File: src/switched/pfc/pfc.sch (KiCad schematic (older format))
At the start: 67 parts, among them J1 AC-input, J2 Conn_01x02, J3 Conn_01x02, Q1 AOT190A60CL‎, U1 AP3917B, U2 bd7692fj

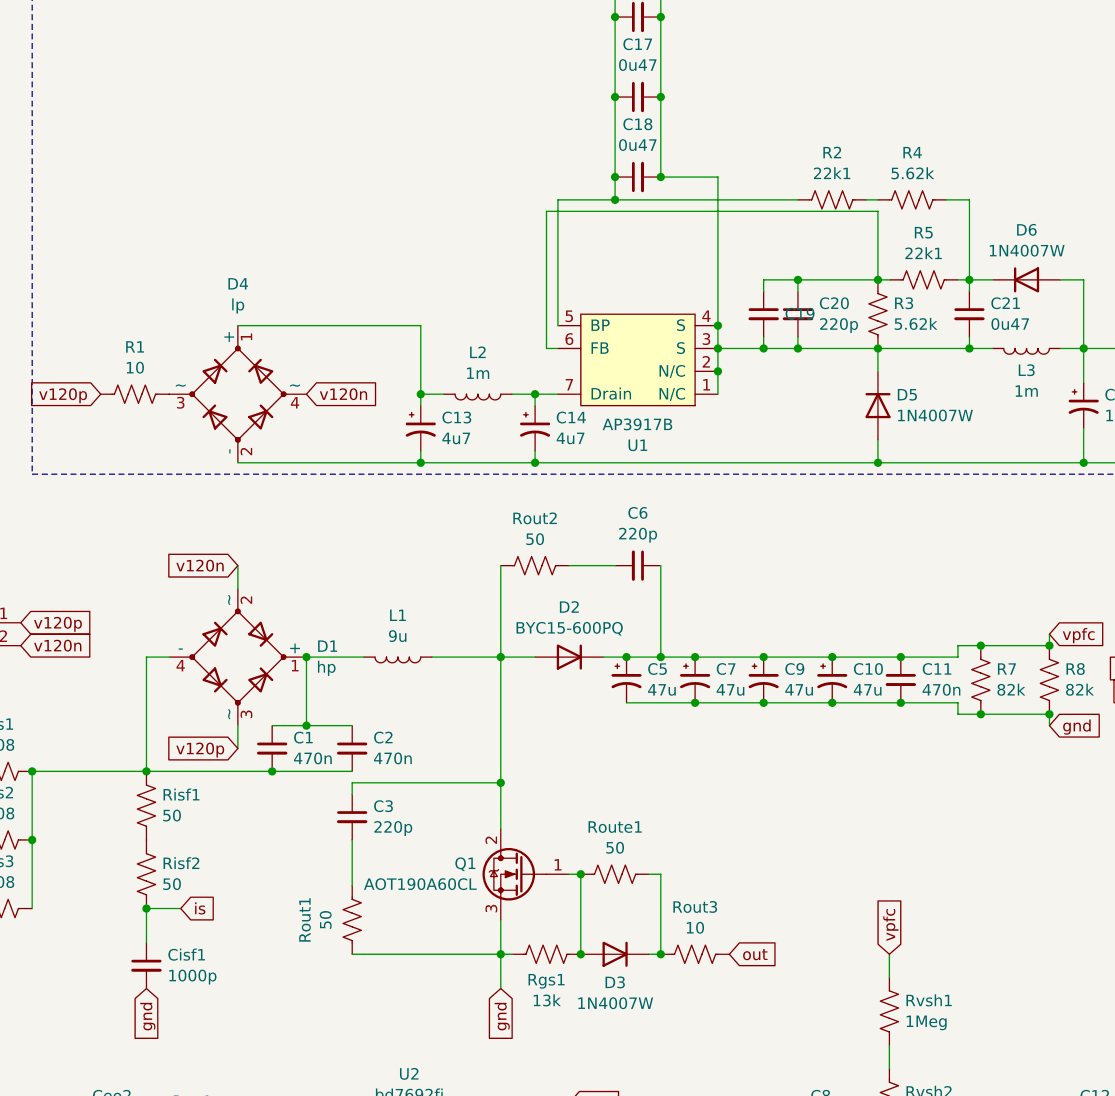
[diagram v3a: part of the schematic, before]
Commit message: fixing the pfc footprints and relating them to their lcsc counterparts
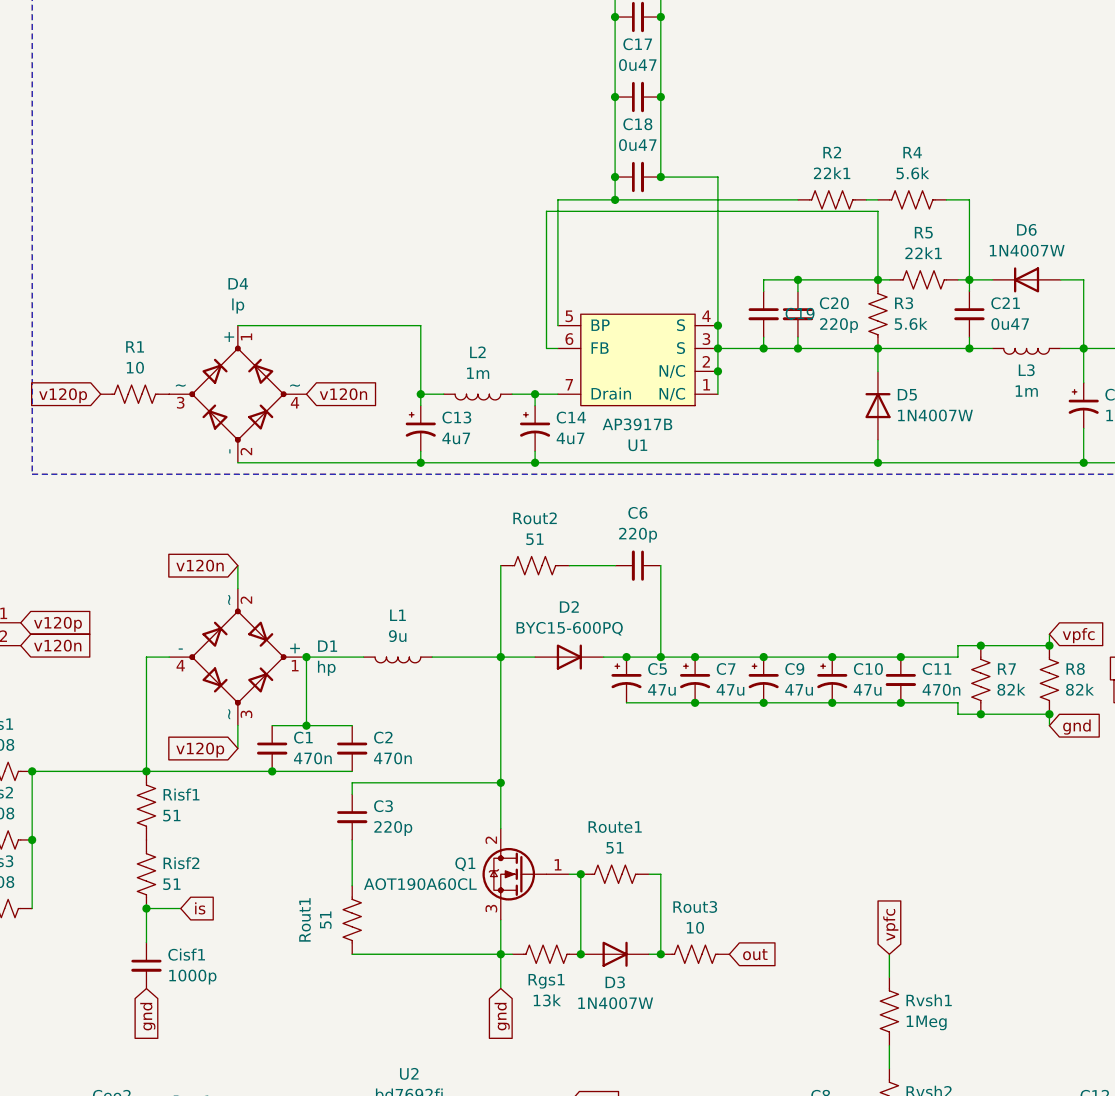
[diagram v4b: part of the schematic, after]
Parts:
- C1, C11, C2: footprint Capacitor_SMD:C_1812_4532Metric_Pad1.57x3.40mm_HandSolder -> Capacitor_SMD:C_1812_4532Metric; Checked yes -> (none); Link (none) -> https://lcsc.com/product-detail/Multilayer-Ceramic-Capacito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; link https://lcsc.com/product-detail/Multilayer-Ceramic-Capacito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 -> (none)
- C10, C5, C7, C9: Link (none) -> https://lcsc.com/product-detail/Aluminum-Electrolytic-Capac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; Working voltage (none) -> 450; link https://lcsc.com/product-detail/Aluminum-Electrolytic-Capac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 -> (none)
- C12, C8, Ceo2, Cisf1: Link (none) -> https://lcsc.com/product-detail/Multilayer-Ceramic-Capacito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; Working voltage (none) -> 50
- C13, C14: Link (none) -> https://lcsc.com/product-detail/Aluminum-Electrolytic-Capac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; Working voltage (none) -> 400; price (none) -> 0.039
- C15, C16, C17, C18, C21, Ceo1: Link (none) -> https://lcsc.com/search?q=CL10B474KA8NNNC; Working voltage (none) -> 25
- C19, C20, C3, C6: Checked yes -> (none); Link (none) -> https://lcsc.com/product-detail/Multilayer-Ceramic-Capacito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; link https://lcsc.com/product-detail/Multilayer-Ceramic-Capacito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 -> (none)
- C22: Link (none) -> https://lcsc.com/product-detail/Aluminum-Electrolytic-Capac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; Working voltage (none) -> 25; price (none) -> 0.0308
- C4: Link (none) -> https://lcsc.com/product-detail/Aluminum-Electrolytic-Capac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; link https://lcsc.com/product-detail/Aluminum-Electrolytic-Capac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 -> (none)
- D1: Link (none) -> https://lcsc.com/product-detail/Bridge-Rectifiers_Yangzhou-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
- D2: Link (none) -> https://lcsc.com/product-detail/Diodes-General-Purpose_WeEn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
- D3, D5, D6: Link (none) -> https://lcsc.com/product-detail/Diodes-General-Purpose_Shan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
- D4: Link (none) -> https://lcsc.com/product-detail/Bridge-Rectifiers_DIYI-Elec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; price 0.6459 -> 0.0342
- J1, J3: Checked (none) -> NA; Link (none) -> NA
- J2: footprint Connector_Wire:SolderWire-2sqmm_1x02_P7.8mm_D2mm_OD3.9mm -> custom:spacedConnector; Checked (none) -> NA; Link (none) -> NA
- L1: Link (none) -> https://www.digikey.com/en/products/detail/ferroxcube/CPV-P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
- L2, L3: Link (none) -> https://lcsc.com/product-detail/Power-Inductors_YJYCOIN-YNR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; price (none) -> 0.0974
- Q1: footprint Package_TO_SOT_THT:TO-220-2_Horizontal_TabDown -> Package_TO_SOT_THT:TO-220-3_Horizontal_TabDown; Link (none) -> https://www.digikey.com/en/products/detail/alpha-omega-semi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; price 2.5648 -> 2.17
- R1: Link (none) -> https://lcsc.com/product-detail/Wirewound-Resistors_CCO-Chi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; Working voltage (none) -> 300; price (none) -> 0.0443
- R2, R5, R6: Link (none) -> https://lcsc.com/product-detail/Metal-Oxide-Resistors_FlyWi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; Working voltage (none) -> 250; price (none) -> 0.0041
- R3, R4: value 5.62k -> 5.6k; footprint Resistor_THT:R_Axial_DIN0309_L9.0mm_D3.2mm_P2.54mm_Vertical -> Resistor_THT:R_Axial_DIN0204_L3.6mm_D1.6mm_P2.54mm_Vertical; Link (none) -> https://lcsc.com/product-detail/Metal-Film-Resistor-TH_5-6K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; Working voltage (none) -> 150; price (none) -> 0.0087
- R7, R8: Link (none) -> https://lcsc.com/product-detail/Metal-Oxide-Resistors_FlyWi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; Working voltage (none) -> 500; price (none) -> 0.0487
- Reo1, Rt1: Link (none) -> https://lcsc.com/product-detail/High-Precision-Low-TCR-SMD-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; Working voltage (none) -> 75
- Rgs1, Rovpl1, Rvsl1, Rvsl2: Link (none) -> https://lcsc.com/product-detail/Chip-Resistor-Surface-Mount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; Working voltage (none) -> 50
- Ris1, Ris2, Ris3: Link (none) -> https://lcsc.com/product-detail/Low-Resistors-Current-Sense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
- Risf1, Risf2, Route1: value 50 -> 51; Link (none) -> https://lcsc.com/product-detail/Carbon-Film-Resistors_Huaxi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; Working voltage (none) -> 250
- Rout1, Rout2: value 50 -> 51; footprint Resistor_SMD:R_1206_3216Metric_Pad1.30x1.75mm_HandSolder -> Resistor_THT:R_Axial_DIN0207_L6.3mm_D2.5mm_P10.16mm_Horizontal; Link (none) -> https://lcsc.com/product-detail/Carbon-Film-Resistors_Huaxi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; Working voltage (none) -> 250
- Rout3: Link (none) -> https://lcsc.com/product-detail/Chip-Resistor-Surface-Mount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; Working voltage (none) -> 75
- Rovph1, Rovph2, Rvsh1, Rvsh2: Link (none) -> https://lcsc.com/product-detail/High-Voltage-Resistor_Ever-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; Working voltage (none) -> 500
- U1: footprint custom:SO-7_5.3x6.2mm_P1.27mm -> custom:SO-7_3.9x4.9mm_P1.27mm; Link (none) -> https://www.digikey.com/en/products/detail/AP3917BS7-13/AP3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; price (none) -> 0.58000
- U2: footprint Package_SO:SOP-8_6.62x9.15mm_P2.54mm -> Package_SO:SOIC-8_3.9x4.9mm_P1.27mm; Link (none) -> https://www.digikey.com/en/products/detail/BD7692FJ-E2/846-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

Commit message: Midterm report
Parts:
- C1, C11, C2: price 0.0143 -> 0.2238
- C10, C5, C7, C9: price 0.6115 -> 0.4815
- C12, C8, Cisf1: price 0.004 -> 0.0031
- C13, C14: price 0.039 -> 0.039
- C15, C16, C17, C18, C21, Ceo1: price 0.0143 -> 0.0112
- C19, C20, C3, C6: price 0.016 -> 0.0126
- C4: price 0.0125 -> 0.0098
- Ceo2: price 0.0041 -> 0.0032
- D1: price 0.6459 -> 0.5086
- D2: price 0.9091 -> 0.7159
- D3, D5, D6: price 0.0086 -> 0.0067
- D4: price 0.0342 -> 0.0271
- L2, L3: price 0.0974 -> 0.0772
- R1: price 0.0443 -> 0.0351
- R2, R5, R6: price 0.0041 -> 0.0041
- R3, R4: price 0.0087 -> 0.0052
- Reo1, Rt1: price 0.0091 -> 0.0071
- Rgs1, Rovpl1, Rvsl1, Rvsl2: price 0.0014 -> 0.0011
- Ris1, Ris2, Ris3: price 0.093 -> 0.0732
- Risf1, Risf2, Rout1, Rout2, Route1: price 0.0064 -> 0.005
- Rout3: price 0.0016 -> 0.0012
- Rovph1, Rovph2, Rvsh1, Rvsh2: price 0.0298 -> 0.0234
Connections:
- net v12 renamed vcc
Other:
- moved on the sheet: C1, C10, C11, C12, C13, C14, C15, C16, C17, C18, C19, C2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

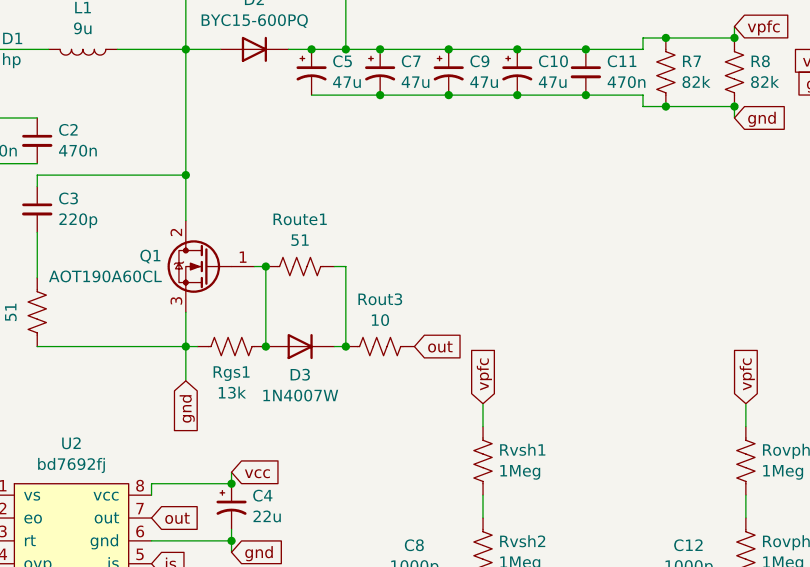
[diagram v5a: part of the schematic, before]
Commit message: Faster gate drive on pfc
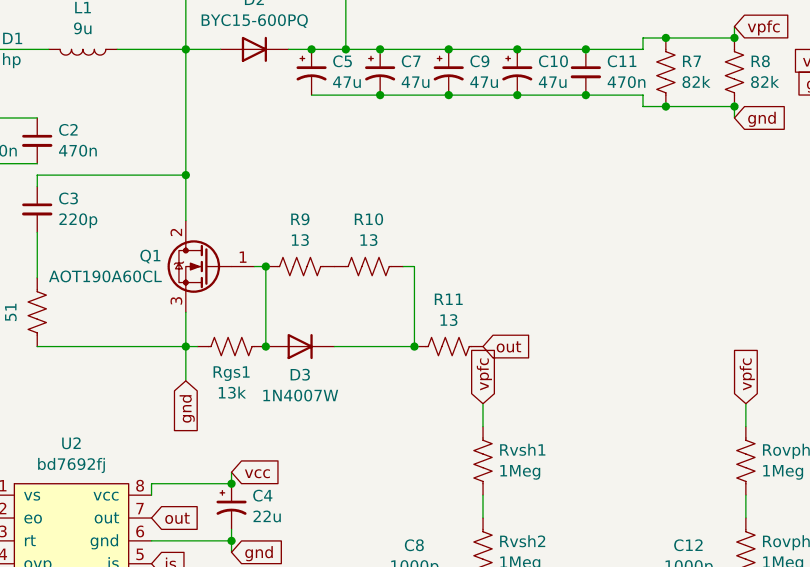
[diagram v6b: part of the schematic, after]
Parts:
- removed Route1: 51, Resistor_THT:R_Axial_DIN0207_L6.3mm_D2.5mm_P2.54mm_Vertical, symbol Device:R_US
- added R10, R9: 13, Resistor_SMD:R_0603_1608Metric_Pad0.98x0.95mm_HandSolder, symbol Device:R_US
- R11: renamed from Rout3; value 10 -> 13; Link https://lcsc.com/product-detail/Chip-Resistor-Surface-Mount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 -> https://lcsc.com/product-detail/High-Precision-Low-TCR-SMD-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; price 0.0012 -> 0.0119
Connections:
- net at D3.2 (A), Q1.1 (G), Rgs1.2: now also R9.1
- net at D3.1 (K), R11.1: now also R10.2
- new net: R10.1, R9.2
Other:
- moved on the sheet: R11
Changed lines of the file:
@@
 	3700 5350 3700 5700
-$Comp
-L Device:R_US Route1
-U 1 1 6037526C
-P 3850 5350
-F 0 "Route1" V 4055 5350 50  0000 C CNN
-F 1 "51" V 3964 5350 50  0000 C CNN
-F 2 "Resistor_THT:R_Axial_DIN0207_L6.3mm_D2.5mm_P2.54mm_Vertical" V 3890 5340 50  0001 C CNN
-F 3 "CF1/4W-51Ω±5%T52" H 3850 5350 50  0001 C CNN
-F 4 "0.005" H 3850 5350 50  0001 C CNN "price"
-F 5 "" H 3850 5350 50  0001 C CNN "Checked"
-F 6 "https://lcsc.com/product-detail/Carbon-Film-Resistors_Huaxing-Mechanical-Elec-CF1-4W-51%CE%A9-5-T52_C714278.html" H 3850 5350 50  0001 C CNN "Link"
-F 7 "250" H 3850 5350 50  0001 C CNN "Working voltage"
-	1    3850 5350
-	0    -1   -1   0
-$EndComp
 $Comp
 L Device:D D3
@@
 $EndComp
 $Comp
-L Device:R_US Rout3
+L Device:R_US R11
 U 1 1 60379771
-P 4200 5700
-F 0 "Rout3" V 4405 5700 50  0000 C CNN
-F 1 "10" V 4314 5700 50  0000 C CNN
-F 2 "Resistor_SMD:R_0603_1608Metric_Pad0.98x0.95mm_HandSolder" V 4240 5690 50  0001 C CNN
-F 3 "WR06X100JTL" H 4200 5700 50  0001 C CNN
-F 4 "0.0012" H 4200 5700 50  0001 C CNN "price"
-F 5 "" H 4200 5700 50  0001 C CNN "Checked"
-F 6 "https://lcsc.com/product-detail/Chip-Resistor-Surface-Mount_Walsin-Tech-Corp-WR06X100JTL_C384297.html" H 4200 5700 50  0001 C CNN "Link"
-F 7 "75" H 4200 5700 50  0001 C CNN "Working voltage"
-	1    4200 5700
+P 4500 5700
+F 0 "R11" V 4705 5700 50  0000 C CNN
+F 1 "13" V 4614 5700 50  0000 C CNN
+F 2 "Resistor_SMD:R_0603_1608Metric_Pad0.98x0.95mm_HandSolder" V 4540 5690 50  0001 C CNN
+F 3 "ARG03FTC0130" H 4500 5700 50  0001 C CNN
+F 4 "0.0119" H 4500 5700 50  0001 C CNN "price"
+F 5 "" H 4500 5700 50  0001 C CNN "Checked"
+F 6 "https://lcsc.com/product-detail/High-Precision-Low-TCR-SMD-Resistors_Viking-Tech-ARG03FTC0130_C217732.html" H 4500 5700 50  0001 C CNN "Link"
+F 7 "75" H 4500 5700 50  0001 C CNN "Working voltage"
+	1    4500 5700
 	0    -1   -1   0
 $EndComp
-Text GLabel 4350 5700 2    50   Input ~ 0
+Text GLabel 4650 5700 2    50   Input ~ 0
 out
 Wire Wire Line
@@
 	1300 5200 1300 5500
 Wire Wire Line
-	4000 5350 4050 5350
-Wire Wire Line
-	4050 5700 4000 5700
-Wire Wire Line
-	4050 5700 4050 5350
-Connection ~ 4050 5700
+	4300 5350 4350 5350
+Wire Wire Line
+	4350 5700 4350 5350
+Connection ~ 4350 5700
 $Comp
 L Device:R_US Rout1
@@
 Wire Wire Line
 	3350 4950 3350 5150
-Connection ~ 3700 5350
 Connection ~ 3700 5700
 Wire Wire Line
@@
 	1    0    0    -1
 $EndComp
+$Comp
+L Device:R_US R9
+U 1 1 604B894B
+P 3850 5350
+F 0 "R9" V 4055 5350 50  0000 C CNN
+F 1 "13" V 3964 5350 50  0000 C CNN
+F 2 "Resistor_SMD:R_0603_1608Metric_Pad0.98x0.95mm_HandSolder" V 3890 5340 50  0001 C CNN
+F 3 "ARG03FTC0130" H 3850 5350 50  0001 C CNN
+F 4 "0.0119" H 3850 5350 50  0001 C CNN "price"
+F 5 "" H 3850 5350 50  0001 C CNN "Checked"
+F 6 "https://lcsc.com/product-detail/High-Precision-Low-TCR-SMD-Resistors_Viking-Tech-ARG03FTC0130_C217732.html" H 3850 5350 50  0001 C CNN "Link"
+F 7 "75" H 3850 5350 50  0001 C CNN "Working voltage"
+	1    3850 5350
+	0    -1   -1   0
+$EndComp
+Connection ~ 3700 5350
+$Comp
+L Device:R_US R10
+U 1 1 604DB3E6
+P 4150 5350
+F 0 "R10" V 4355 5350 50  0000 C CNN
+F 1 "13" V 4264 5350 50  0000 C CNN
+F 2 "Resistor_SMD:R_0603_1608Metric_Pad0.98x0.95mm_HandSolder" V 4190 5340 50  0001 C CNN
+F 3 "ARG03FTC0130" H 4150 5350 50  0001 C CNN
+F 4 "0.0119" H 4150 5350 50  0001 C CNN "price"
+F 5 "" H 4150 5350 50  0001 C CNN "Checked"
+F 6 "https://lcsc.com/product-detail/High-Precision-Low-TCR-SMD-Resistors_Viking-Tech-ARG03FTC0130_C217732.html" H 4150 5350 50  0001 C CNN "Link"
+F 7 "75" H 4150 5350 50  0001 C CNN "Working voltage"
+	1    4150 5350
+	0    -1   -1   0
+$EndComp
+Wire Wire Line
+	4000 5700 4350 5700
 $EndSCHEMATC
